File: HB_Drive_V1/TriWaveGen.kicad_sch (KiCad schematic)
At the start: 0 parts

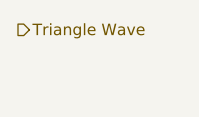
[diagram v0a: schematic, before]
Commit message: fixes git and adds a first revision of the Inner Current Regulator (NOT COMPLETE)
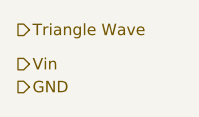
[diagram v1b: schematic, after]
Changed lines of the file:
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@@
+		)
+	)
+	(hierarchical_label "GND"
+		(shape output)
+		(at 139.7 82.55 0)
+		(effects
+			(font
+				(size 1.27 1.27)
+			)
+			(justify left)
+		)
+	)
+	(hierarchical_label "Vin"
+		(shape output)
+		(at 139.7 80.01 0)
+		(effects
+			(font
+				(size 1.27 1.27)
+			)
+			(justify left)
 		)
 	)
